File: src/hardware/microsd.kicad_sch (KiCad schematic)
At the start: 12 parts

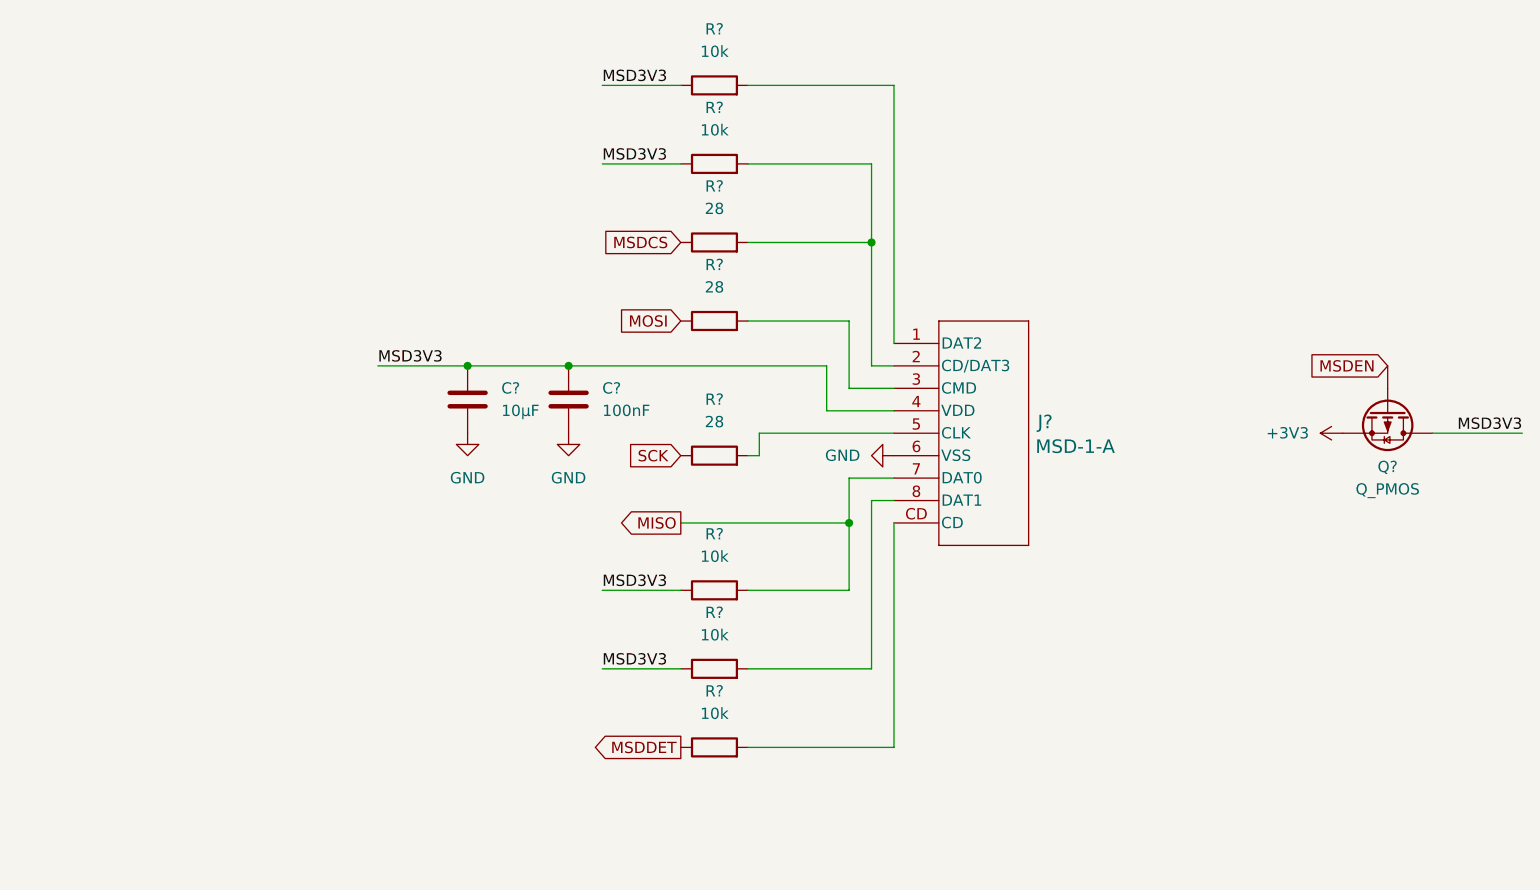
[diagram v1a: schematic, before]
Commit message: Replaced schematics, 3d models and footprints. Added vibration motor.
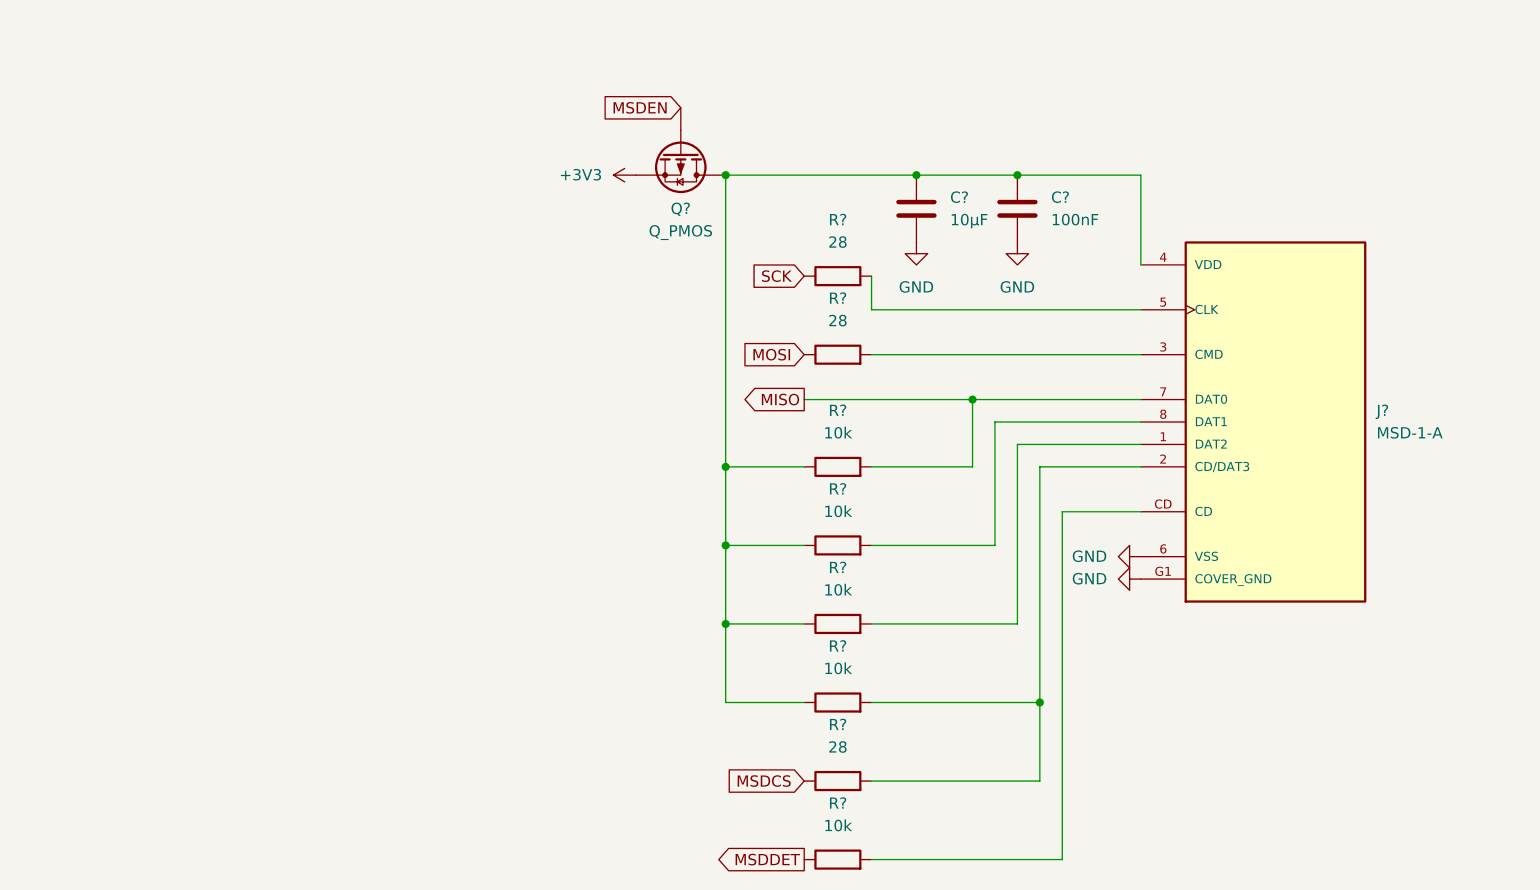
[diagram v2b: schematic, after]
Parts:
- removed J?: MSD-1-A, CONN9_MSD-1_CUD, symbol MSD-1-A:MSD-1-A
- added J?: MSD-1-A, MSD-1-A:CUI_MSD-1-A, symbol MSD-1-A:MSD-1-A
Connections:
- net MISO: now also J?.7 (DAT0)
- net at R?.2: now also J?.1 (DAT2)
- net at R?.2, R?.2: now also J?.2 (CD/DAT3)
- net at R?.2: now also J?.3 (CMD)
- net at R?.2: now also J?.5 (CLK)
- net at R?.2: now also J?.8 (DAT1)
- net at R?.2: now also J?.CD
- net GND renamed COVER_GND
- net COVER_GND: now also J?.6 (VSS), J?.G1 (COVER_GND), J?.G2 (COVER_GND), J?.G3 (COVER_GND), J?.G4 (COVER_GND)
- net MSD3V3: no longer names the net of C?.1, C?.1, Q?.D, R?.1, R?.1, R?.1, R?.1
- net MSD3V3: now also J?.4 (VDD)
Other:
- moved on the sheet: C?, Q?, R?

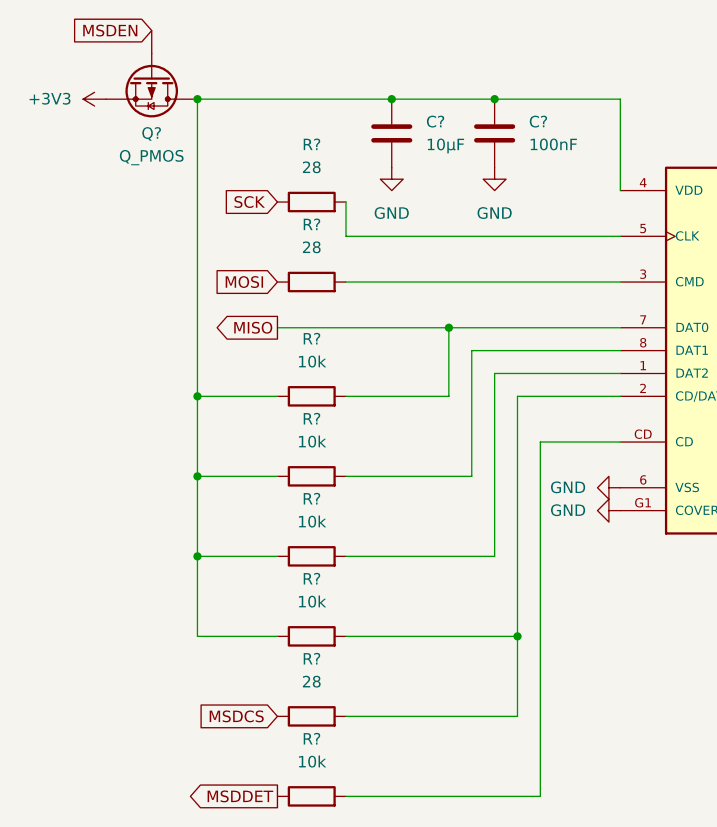
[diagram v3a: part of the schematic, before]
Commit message: Added Accelerometer Clock; Cleanup & Fixes
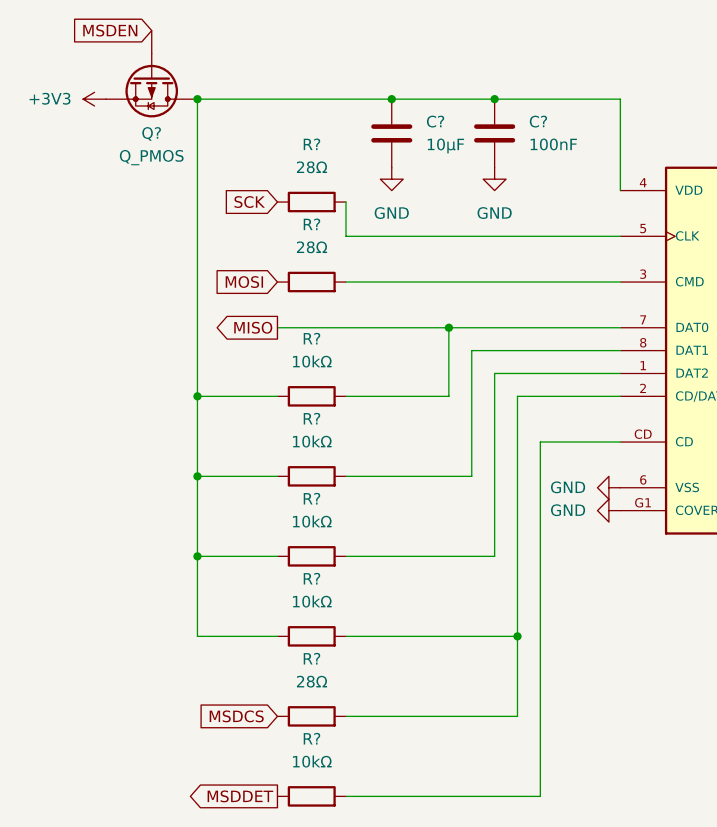
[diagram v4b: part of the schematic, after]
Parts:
- R? (x5): value 10k -> 10kΩ
- R? (x3): value 28 -> 28Ω
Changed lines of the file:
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@@
 			)
 		)
-		(property "Value" "10k"
+		(property "Value" "10kΩ"
 			(at 134.62 116.84 90)
 			(effects
@@
 			)
 		)
-		(property "Value" "10k"
+		(property "Value" "10kΩ"
 			(at 134.62 143.51 90)
 			(effects
@@
 			)
 		)
-		(property "Value" "10k"
+		(property "Value" "10kΩ"
 			(at 134.62 107.95 90)
 			(effects
@@
 			)
 		)
-		(property "Value" "28"
+		(property "Value" "28Ω"
 			(at 134.62 86.36 90)
 			(effects
@@
 			)
 		)
-		(property "Value" "10k"
+		(property "Value" "10kΩ"
 			(at 134.62 125.73 90)
 			(effects
@@
 			)
 		)
-		(property "Value" "10k"
+		(property "Value" "10kΩ"
 			(at 134.62 99.06 90)
 			(effects
@@
 			)
 		)
-		(property "Value" "28"
+		(property "Value" "28Ω"
 			(at 134.62 134.62 90)
 			(effects
@@
 			)
 		)
-		(property "Value" "28"
+		(property "Value" "28Ω"
 			(at 134.62 77.47 90)
 			(effects

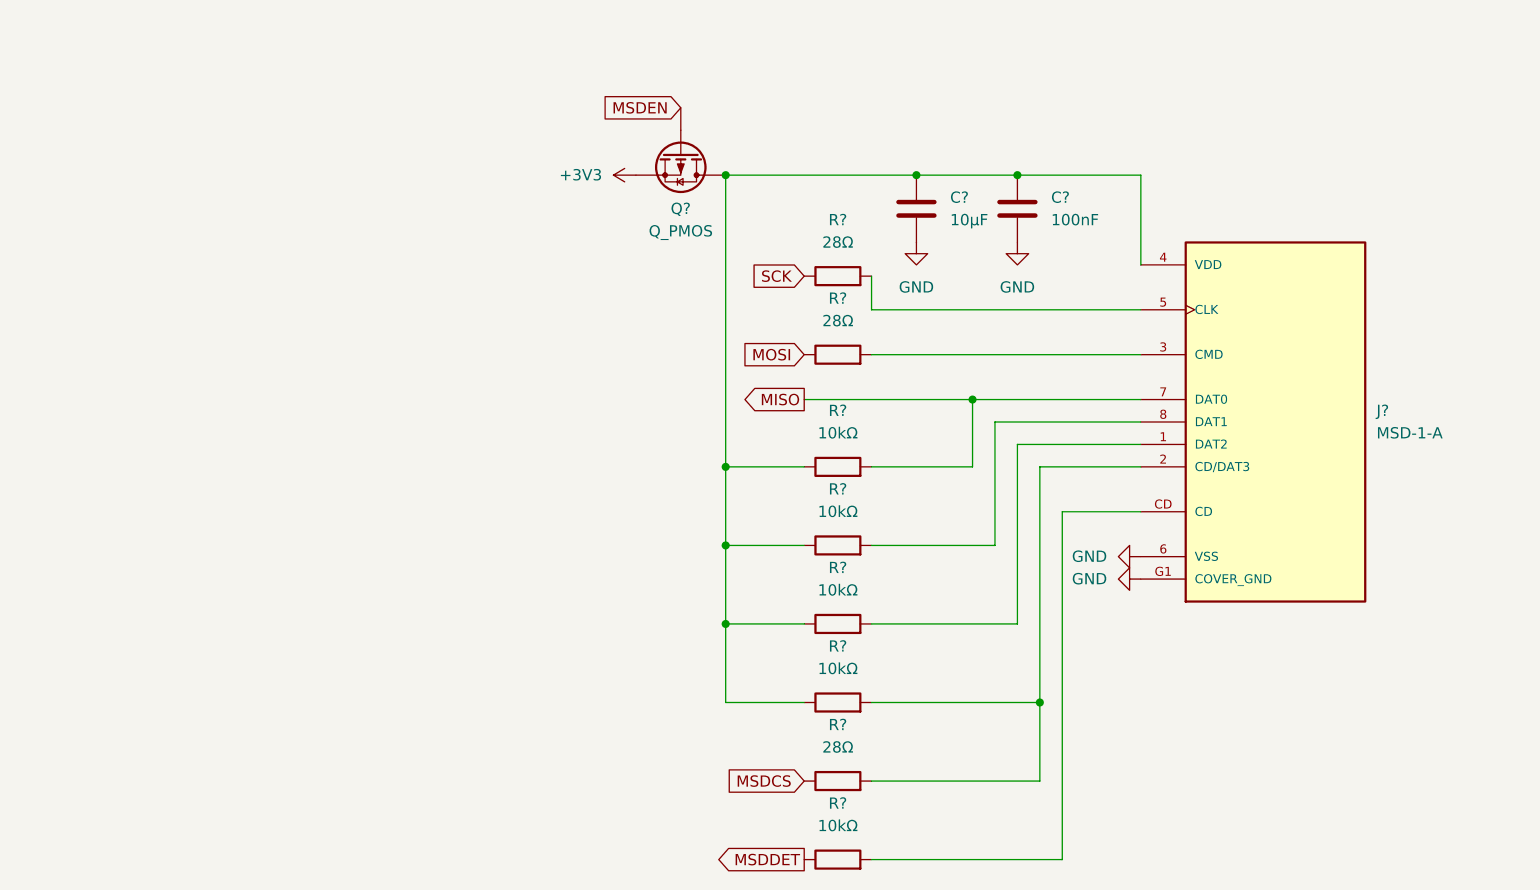
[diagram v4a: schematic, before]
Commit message: Cleanup & Fixes; Added footprints; Removed Light sensors
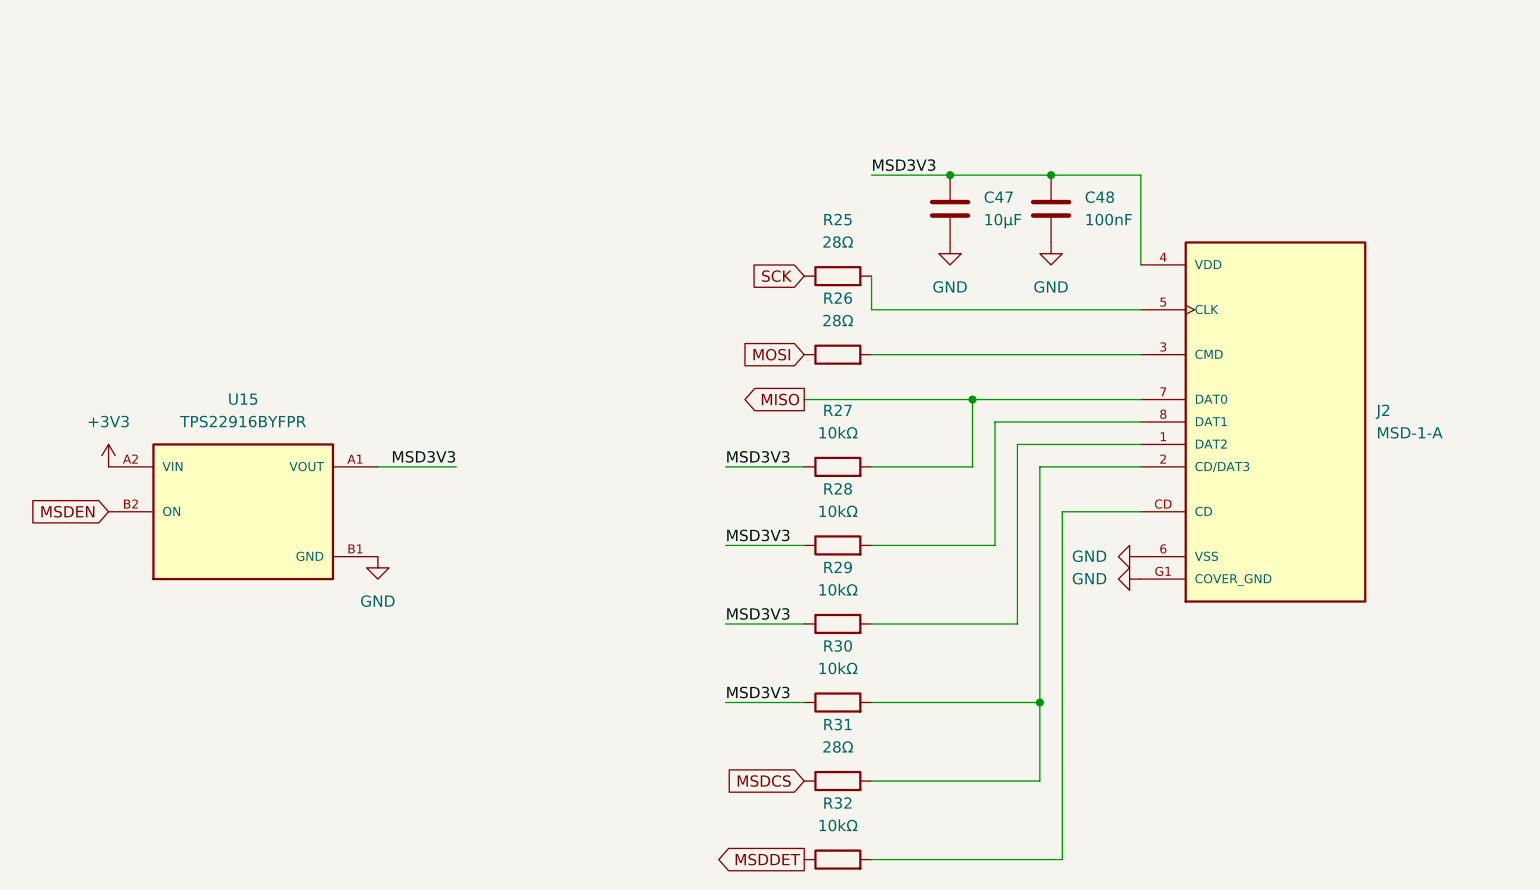
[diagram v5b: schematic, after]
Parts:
- removed Q?: Q_PMOS, symbol Device:Q_PMOS
- added U15: TPS22916BYFPR, Project:IC_TPS22916BYFPR, symbol TPS22916BYFPR:TPS22916BYFPR
- C47, C48: renamed from C?; footprint (none) -> Capacitor_SMD:C_0603_1608Metric
- J2: renamed from J?; footprint MSD-1-A:CUI_MSD-1-A -> Project:CUI_MSD-1-A
- R25, R26, R27, R28, R29, R30, R31, R32: renamed from R?; footprint (none) -> Resistor_SMD:R_0603_1608Metric
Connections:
- net +3V3: now also U15.A2 (VIN)
- net COVER_GND: now also U15.B1 (GND)
- net MSDEN: now also U15.B2 (ON)
- net MSD3V3: now reaches C47.1, C48.1, J2.4 (VDD), R27.1, R28.1, R29.1, R30.1
- net MSD3V3: now also U15.A1 (VOUT)
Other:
- moved on the sheet: C47, C48

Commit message: Cleanup & Fixes; Changed GPIO; Added Camera; Added Microphone
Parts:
- renumbered C47 to C45, C48 to C46, R25 to R23, R26 to R24, R27 to R25, R28 to R26, R29 to R27, R30 to R28, R31 to R29, R32 to R30
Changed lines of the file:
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@@
 		(dnp no)
 		(fields_autoplaced yes)
-		(property "Reference" "R29"
+		(property "Reference" "R27"
 			(at 134.62 114.3 90)
 			(effects
@@
 			(project "raywatch"
 				(path "/7b654ee8-2a53-4d39-8b7d-32c7bb3cb0ed/d3a87cc9-ac13-45e7-bf56-8d3ed6c53cc2"
-					(reference "R29")
+					(reference "R27")
 					(unit 1)
 				)
@@
 		(dnp no)
 		(fields_autoplaced yes)
-		(property "Reference" "#PWR0298"
+		(property "Reference" "#PWR0294"
 			(at 158.75 83.82 0)
 			(effects
@@
 			(project "raywatch"
 				(path "/7b654ee8-2a53-4d39-8b7d-32c7bb3cb0ed/d3a87cc9-ac13-45e7-bf56-8d3ed6c53cc2"
-					(reference "#PWR0298")
+					(reference "#PWR0294")
 					(unit 1)
 				)
@@
 		(dnp no)
 		(fields_autoplaced yes)
-		(property "Reference" "#PWR0299"
+		(property "Reference" "#PWR0295"
 			(at 162.56 113.03 0)
 			(effects
@@
 			(project "raywatch"
 				(path "/7b654ee8-2a53-4d39-8b7d-32c7bb3cb0ed/d3a87cc9-ac13-45e7-bf56-8d3ed6c53cc2"
-					(reference "#PWR0299")
+					(reference "#PWR0295")
 					(unit 1)
 				)
@@
 		(dnp no)
 		(fields_autoplaced yes)
-		(property "Reference" "#PWR0295"
+		(property "Reference" "#PWR0291"
 			(at 52.07 106.68 0)
 			(effects
@@
 			(project "raywatch"
 				(path "/7b654ee8-2a53-4d39-8b7d-32c7bb3cb0ed/d3a87cc9-ac13-45e7-bf56-8d3ed6c53cc2"
-					(reference "#PWR0295")
+					(reference "#PWR0291")
 					(unit 1)
 				)
@@
 		(dnp no)
 		(fields_autoplaced yes)
-		(property "Reference" "#PWR0296"
+		(property "Reference" "#PWR0292"
 			(at 82.55 119.38 0)
 			(effects
@@
 			(project "raywatch"
 				(path "/7b654ee8-2a53-4d39-8b7d-32c7bb3cb0ed/d3a87cc9-ac13-45e7-bf56-8d3ed6c53cc2"
-					(reference "#PWR0296")
+					(reference "#PWR0292")
 					(unit 1)
 				)
@@
 		(dnp no)
 		(fields_autoplaced yes)
-		(property "Reference" "R32"
+		(property "Reference" "R30"
 			(at 134.62 140.97 90)
 			(effects
@@
 			(project "raywatch"
 				(path "/7b654ee8-2a53-4d39-8b7d-32c7bb3cb0ed/d3a87cc9-ac13-45e7-bf56-8d3ed6c53cc2"
-					(reference "R32")
+					(reference "R30")
 					(unit 1)
 				)
@@
 		(dnp no)
 		(fields_autoplaced yes)
-		(property "Reference" "#PWR0297"
+		(property "Reference" "#PWR0293"
 			(at 147.32 83.82 0)
 			(effects
@@
 			(project "raywatch"
 				(path "/7b654ee8-2a53-4d39-8b7d-32c7bb3cb0ed/d3a87cc9-ac13-45e7-bf56-8d3ed6c53cc2"
-					(reference "#PWR0297")
+					(reference "#PWR0293")
 					(unit 1)
 				)
@@
 		(dnp no)
 		(fields_autoplaced yes)
-		(property "Reference" "R28"
+		(property "Reference" "R26"
 			(at 134.62 105.41 90)
 			(effects
@@
 			(project "raywatch"
 				(path "/7b654ee8-2a53-4d39-8b7d-32c7bb3cb0ed/d3a87cc9-ac13-45e7-bf56-8d3ed6c53cc2"
-					(reference "R28")
+					(reference "R26")
 					(unit 1)
 				)
@@
 		(dnp no)
 		(fields_autoplaced yes)
-		(property "Reference" "C47"
+		(property "Reference" "C45"
 			(at 151.13 72.3899 0)
 			(effects
@@
 			(project "raywatch"
 				(path "/7b654ee8-2a53-4d39-8b7d-32c7bb3cb0ed/d3a87cc9-ac13-45e7-bf56-8d3ed6c53cc2"
-					(reference "C47")
+					(reference "C45")
 					(unit 1)
 				)
@@
 		(dnp no)
 		(fields_autoplaced yes)
-		(property "Reference" "R26"
+		(property "Reference" "R24"
 			(at 134.62 83.82 90)
 			(effects
@@
 			(project "raywatch"
 				(path "/7b654ee8-2a53-4d39-8b7d-32c7bb3cb0ed/d3a87cc9-ac13-45e7-bf56-8d3ed6c53cc2"
-					(reference "R26")
+					(reference "R24")
 					(unit 1)
 				)
@@
 		(dnp no)
 		(fields_autoplaced yes)
-		(property "Reference" "C48"
+		(property "Reference" "C46"
 			(at 162.56 72.3899 0)
 			(effects
@@
 			(project "raywatch"
 				(path "/7b654ee8-2a53-4d39-8b7d-32c7bb3cb0ed/d3a87cc9-ac13-45e7-bf56-8d3ed6c53cc2"
-					(reference "C48")
+					(reference "C46")
 					(unit 1)
 				)
@@
 		(dnp no)
 		(fields_autoplaced yes)
-		(property "Reference" "#PWR0300"
+		(property "Reference" "#PWR0296"
 			(at 162.56 115.57 0)
 			(effects
@@
 			(project "raywatch"
 				(path "/7b654ee8-2a53-4d39-8b7d-32c7bb3cb0ed/d3a87cc9-ac13-45e7-bf56-8d3ed6c53cc2"
-					(reference "#PWR0300")
+					(reference "#PWR0296")
 					(unit 1)
 				)
@@
 		(dnp no)
 		(fields_autoplaced yes)
-		(property "Reference" "R30"
+		(property "Reference" "R28"
 			(at 134.62 123.19 90)
 			(effects
@@
 			(project "raywatch"
 				(path "/7b654ee8-2a53-4d39-8b7d-32c7bb3cb0ed/d3a87cc9-ac13-45e7-bf56-8d3ed6c53cc2"
-					(reference "R30")
+					(reference "R28")
 					(unit 1)
 				)
@@
 		(dnp no)
 		(fields_autoplaced yes)
-		(property "Reference" "R27"
+		(property "Reference" "R25"
 			(at 134.62 96.52 90)
 			(effects
@@
 			(project "raywatch"
 				(path "/7b654ee8-2a53-4d39-8b7d-32c7bb3cb0ed/d3a87cc9-ac13-45e7-bf56-8d3ed6c53cc2"
-					(reference "R27")
+					(reference "R25")
 					(unit 1)
 				)
@@
 		(dnp no)
 		(fields_autoplaced yes)
-		(property "Reference" "R31"
+		(property "Reference" "R29"
 			(at 134.62 132.08 90)
 			(effects
@@
 			(project "raywatch"
 				(path "/7b654ee8-2a53-4d39-8b7d-32c7bb3cb0ed/d3a87cc9-ac13-45e7-bf56-8d3ed6c53cc2"
-					(reference "R31")
+					(reference "R29")
 					(unit 1)
 				)
@@
 		(dnp no)
 		(fields_autoplaced yes)
-		(property "Reference" "R25"
+		(property "Reference" "R23"
 			(at 134.62 74.93 90)
 			(effects
@@
 			(project "raywatch"
 				(path "/7b654ee8-2a53-4d39-8b7d-32c7bb3cb0ed/d3a87cc9-ac13-45e7-bf56-8d3ed6c53cc2"
-					(reference "R25")
-					(unit 1)
-				)
+					(reference "R23")
+					(unit 1)
+				)
